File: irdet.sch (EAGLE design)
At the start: 70 parts, among them IC1 MEGA8-AI, IC2 78L05F, IC3 78L08F, J1 PSH02-04WG, J2 PSH02-04WG, J3 PSH02-04WG, J4 PSH02-04WG, J5 22-05-7098-09, T1 BC847, T2 BC857, T3 BC847, T4 BC857, T5 BC847, T6 BC857, T7 BC847, T8 BC857, X1 MVE252-5-V, X2 MVE252-5-V

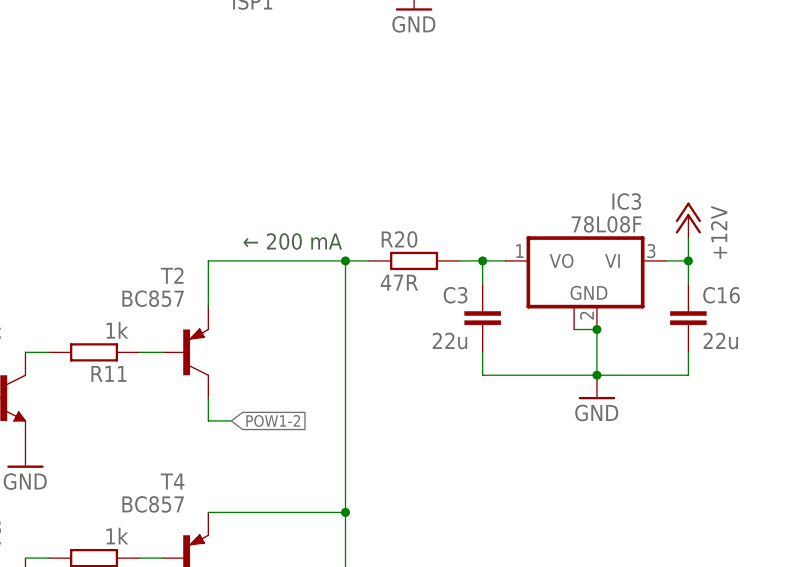
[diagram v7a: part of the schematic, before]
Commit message: Change IR resistor to 33R (~200 mA).
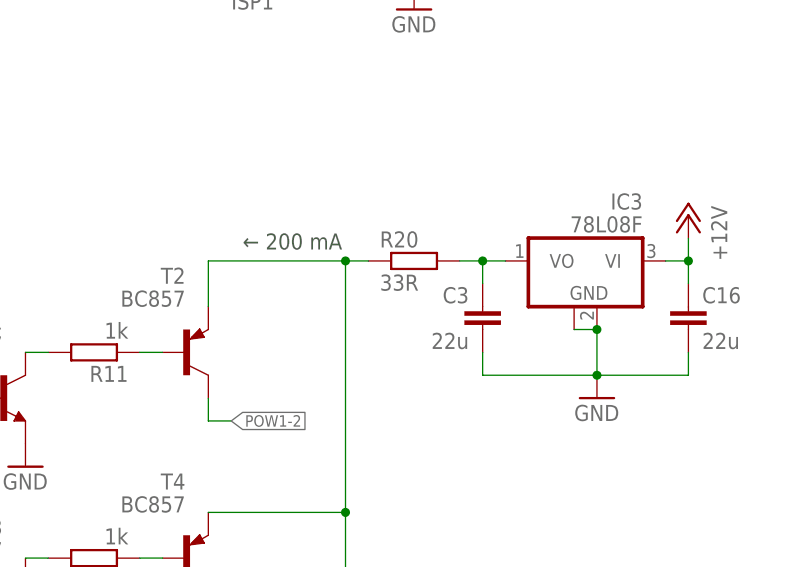
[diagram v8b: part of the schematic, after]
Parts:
- R20: value 47R -> 33R
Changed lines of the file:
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@@
 <grid distance="0.1" unitdist="inch" unit="inch" style="dots" multiple="2" display="no" altdistance="0.05" altunitdist="inch" altunit="inch"/>
 <layers>
-<layer number="1" name="Top" color="3" fill="1" visible="yes" active="no"/>
-<layer number="2" name="Route2" color="16" fill="1" visible="yes" active="no"/>
-<layer number="3" name="Route3" color="17" fill="1" visible="yes" active="no"/>
-<layer number="4" name="Route4" color="18" fill="1" visible="yes" active="no"/>
-<layer number="5" name="Route5" color="19" fill="1" visible="yes" active="no"/>
-<layer number="6" name="Route6" color="25" fill="1" visible="yes" active="no"/>
-<layer number="7" name="Route7" color="26" fill="1" visible="yes" active="no"/>
-<layer number="8" name="Route8" color="27" fill="1" visible="yes" active="no"/>
-<layer number="9" name="Route9" color="28" fill="1" visible="yes" active="no"/>
-<layer number="10" name="Route10" color="29" fill="1" visible="yes" active="no"/>
-<layer number="11" name="Route11" color="30" fill="1" visible="yes" active="no"/>
-<layer number="12" name="Route12" color="20" fill="1" visible="yes" active="no"/>
-<layer number="13" name="Route13" color="21" fill="1" visible="yes" active="no"/>
-<layer number="14" name="Route14" color="22" fill="1" visible="yes" active="no"/>
-<layer number="15" name="Route15" color="23" fill="1" visible="yes" active="no"/>
-<layer number="16" name="Bottom" color="4" fill="1" visible="yes" active="no"/>
-<layer number="17" name="Pads" color="2" fill="1" visible="yes" active="no"/>
-<layer number="18" name="Vias" color="2" fill="1" visible="yes" active="no"/>
-<layer number="19" name="Unrouted" color="6" fill="1" visible="yes" active="no"/>
-<layer number="20" name="Dimension" color="24" fill="1" visible="yes" active="no"/>
-<layer number="21" name="tPlace" color="7" fill="1" visible="yes" active="no"/>
-<layer number="22" name="bPlace" color="7" fill="1" visible="yes" active="no"/>
-<layer number="23" name="tOrigins" color="15" fill="1" visible="yes" active="no"/>
-<layer number="24" name="bOrigins" color="15" fill="1" visible="yes" active="no"/>
-<layer number="25" name="tNames" color="7" fill="1" visible="yes" active="no"/>
-<layer number="26" name="bNames" color="7" fill="1" visible="yes" active="no"/>
-<layer number="27" name="tValues" color="7" fill="1" visible="yes" active="no"/>
-<layer number="28" name="bValues" color="7" fill="1" visible="yes" active="no"/>
+<layer number="1" name="Top" color="3" fill="1" visible="no" active="no"/>
+<layer number="2" name="Route2" color="16" fill="1" visible="no" active="no"/>
+<layer number="3" name="Route3" color="17" fill="1" visible="no" active="no"/>
+<layer number="4" name="Route4" color="18" fill="1" visible="no" active="no"/>
+<layer number="5" name="Route5" color="19" fill="1" visible="no" active="no"/>
+<layer number="6" name="Route6" color="25" fill="1" visible="no" active="no"/>
+<layer number="7" name="Route7" color="26" fill="1" visible="no" active="no"/>
+<layer number="8" name="Route8" color="27" fill="1" visible="no" active="no"/>
+<layer number="9" name="Route9" color="28" fill="1" visible="no" active="no"/>
+<layer number="10" name="Route10" color="29" fill="1" visible="no" active="no"/>
+<layer number="11" name="Route11" color="30" fill="1" visible="no" active="no"/>
+<layer number="12" name="Route12" color="20" fill="1" visible="no" active="no"/>
+<layer number="13" name="Route13" color="21" fill="1" visible="no" active="no"/>
+<layer number="14" name="Route14" color="22" fill="1" visible="no" active="no"/>
+<layer number="15" name="Route15" color="23" fill="1" visible="no" active="no"/>
+<layer number="16" name="Bottom" color="4" fill="1" visible="no" active="no"/>
+<layer number="17" name="Pads" color="2" fill="1" visible="no" active="no"/>
+<layer number="18" name="Vias" color="2" fill="1" visible="no" active="no"/>
+<layer number="19" name="Unrouted" color="6" fill="1" visible="no" active="no"/>
+<layer number="20" name="Dimension" color="24" fill="1" visible="no" active="no"/>
+<layer number="21" name="tPlace" color="7" fill="1" visible="no" active="no"/>
+<layer number="22" name="bPlace" color="7" fill="1" visible="no" active="no"/>
+<layer number="23" name="tOrigins" color="15" fill="1" visible="no" active="no"/>
+<layer number="24" name="bOrigins" color="15" fill="1" visible="no" active="no"/>
+<layer number="25" name="tNames" color="7" fill="1" visible="no" active="no"/>
+<layer number="26" name="bNames" color="7" fill="1" visible="no" active="no"/>
+<layer number="27" name="tValues" color="7" fill="1" visible="no" active="no"/>
+<layer number="28" name="bValues" color="7" fill="1" visible="no" active="no"/>
 <layer number="29" name="tStop" color="7" fill="3" visible="no" active="no"/>
 <layer number="30" name="bStop" color="7" fill="6" visible="no" active="no"/>
@@
 <layer number="35" name="tGlue" color="7" fill="4" visible="no" active="no"/>
 <layer number="36" name="bGlue" color="7" fill="5" visible="no" active="no"/>
-<layer number="37" name="tTest" color="7" fill="1" visible="yes" active="no"/>
-<layer number="38" name="bTest" color="7" fill="1" visible="yes" active="no"/>
+<layer number="37" name="tTest" color="7" fill="1" visible="no" active="no"/>
+<layer number="38" name="bTest" color="7" fill="1" visible="no" active="no"/>
 <layer number="39" name="tKeepout" color="4" fill="11" visible="no" active="no"/>
 <layer number="40" name="bKeepout" color="1" fill="11" visible="no" active="no"/>
@@
 <layer number="44" name="Drills" color="7" fill="1" visible="no" active="no"/>
 <layer number="45" name="Holes" color="7" fill="1" visible="no" active="no"/>
-<layer number="46" name="Milling" color="3" fill="1" visible="yes" active="no"/>
-<layer number="47" name="Measures" color="7" fill="1" visible="yes" active="no"/>
-<layer number="48" name="Document" color="7" fill="1" visible="yes" active="no"/>
-<layer number="49" name="Reference" color="7" fill="1" visible="yes" active="no"/>
-<layer number="50" name="dxf" color="7" fill="1" visible="yes" active="no"/>
-<layer number="51" name="tDocu" color="7" fill="1" visible="yes" active="no"/>
-<layer number="52" name="bDocu" color="7" fill="1" visible="yes" active="no"/>
-<layer number="53" name="tGND_GNDA" color="7" fill="9" visible="yes" active="no"/>
-<layer number="54" name="bGND_GNDA" color="1" fill="9" visible="yes" active="no"/>
-<layer number="56" name="wert" color="7" fill="1" visible="yes" active="no"/>
-<layer number="57" name="tCAD" color="7" fill="1" visible="yes" active="no"/>
-<layer number="59" name="tCarbon" color="7" fill="1" visible="yes" active="no"/>
-<layer number="60" name="bCarbon" color="7" fill="1" visible="yes" active="no"/>
+<layer number="46" name="Milling" color="3" fill="1" visible="no" active="no"/>
+<layer number="47" name="Measures" color="7" fill="1" visible="no" active="no"/>
+<layer number="48" name="Document" color="7" fill="1" visible="no" active="no"/>
+<layer number="49" name="Reference" color="7" fill="1" visible="no" active="no"/>
+<layer number="50" name="dxf" color="7" fill="1" visible="no" active="no"/>
+<layer number="51" name="tDocu" color="7" fill="1" visible="no" active="no"/>
+<layer number="52" name="bDocu" color="7" fill="1" visible="no" active="no"/>
+<layer number="53" name="tGND_GNDA" color="7" fill="9" visible="no" active="no"/>
+<layer number="54" name="bGND_GNDA" color="1" fill="9" visible="no" active="no"/>
+<layer number="56" name="wert" color="7" fill="1" visible="no" active="no"/>
+<layer number="57" name="tCAD" color="7" fill="1" visible="no" active="no"/>
+<layer number="59" name="tCarbon" color="7" fill="1" visible="no" active="no"/>
+<layer number="60" name="bCarbon" color="7" fill="1" visible="no" active="no"/>
 <layer number="88" name="SimResults" color="9" fill="1" visible="yes" active="yes"/>
 <layer number="89" name="SimProbes" color="9" fill="1" visible="yes" active="yes"/>
@@
 </part>
 <part name="GND30" library="supply1" library_urn="urn:adsk.eagle:library:371" deviceset="GND" device=""/>
-<part name="R20" library="rcl" library_urn="urn:adsk.eagle:library:334" deviceset="R-EU_" device="R2010" package3d_urn="urn:adsk.eagle:package:23551/2" value="47R"/>
+<part name="R20" library="rcl" library_urn="urn:adsk.eagle:library:334" deviceset="R-EU_" device="R2010" package3d_urn="urn:adsk.eagle:package:23551/2" value="33R"/>
 </parts>
 <sheets>
